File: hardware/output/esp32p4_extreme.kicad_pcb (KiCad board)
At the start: 4 copper layers, 110 x 80 mm, 234 parts, among them J1 USB-C, J2 USB-C, J3 USB-C, J4 RJ45 MagJack, J5 microSD, J6 2x12 header, J7 Fan 4P, J8 JST-SH 2P, J9 2x8 header, Q1 MMDT3904, Q2 AO3401A, Q3 AO3400A, Q4 AO3401A, Q5 AO3400A, Q6 AO3401A, SW1 Tactile, SW2 Tactile, U1 ESP32-P4NRW32X, U10 TPD4E05U06, U11 TPD4E05U06, U2 W25Q256JV 32MB, U3 TPS62130, U4 TLV62569, U5 LAN8720A, U6 CP2102N, U7 TPD2EUSB30, U8 USBLC6-2SC6, U9 USBLC6-2SC6, Y1 40MHz 10ppm, Y2 25MHz

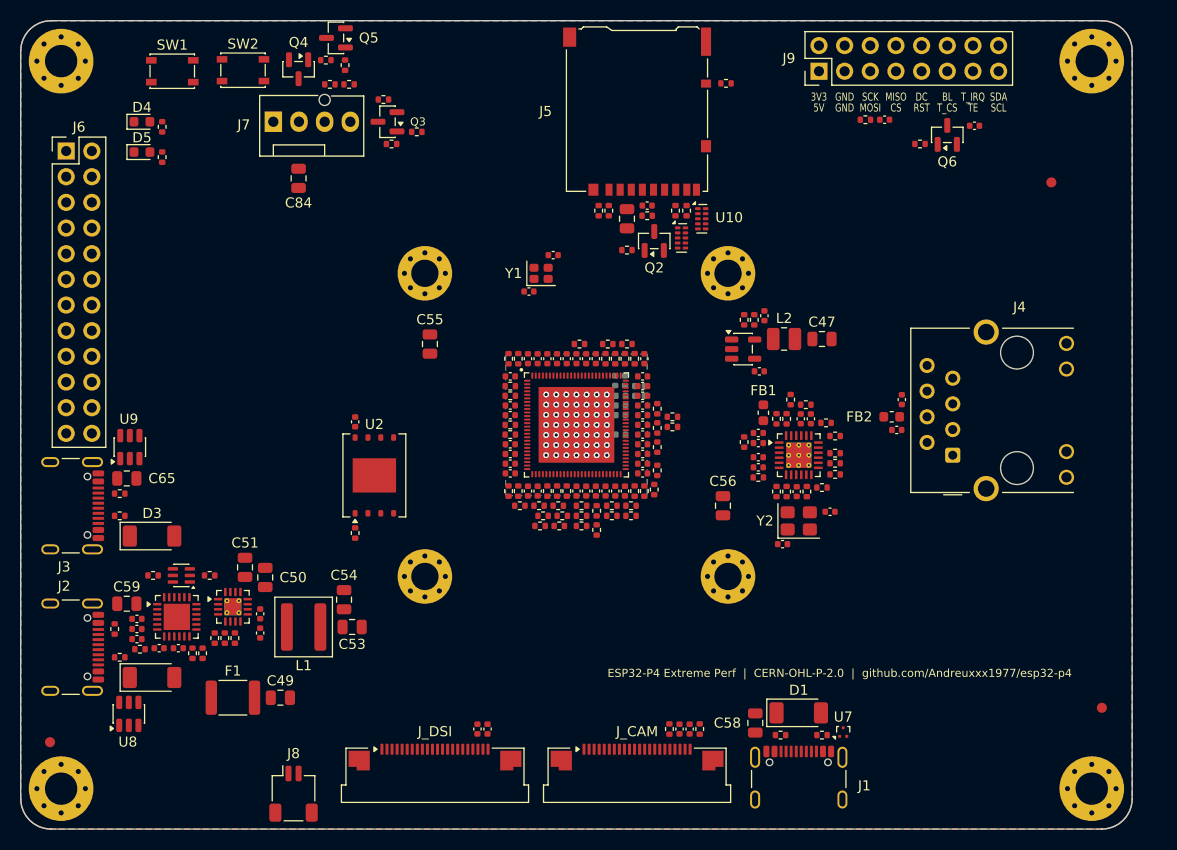
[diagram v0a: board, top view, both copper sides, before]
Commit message: Placement: keep a routable escape channel for every SoC pad; USB-C design tests
The first autorouting runs showed the SoC could not be escaped: the 0402 ring around
the 0.35 mm-pitch QFN left no gap >= 0.35 mm on any side, while ~60 of the 100 connected
pads go to parts outside it.

- layout_plan: new escape-channel model (section 5b). Each connected U1 pad gets a
  straight radial channel from the end of its fan-out stub; a top-side placement near
  the SoC is legal only if, per side and radial band, all channels still pack between
  the other nets' pads at netclass width + clearance (with a bounded 45-degree jog).
  Supply channels end at their first cap; series 0R/22R parts pass their own chain.
  U1 parts must sit in line with their own pad. The Hungarian ring-slot solver is
  replaced by the Near search under these rules (HF caps first).
- board_spec: first cap per pad within 2.1 mm, bulk caps within 4 mm, bias/strap
  within 7 mm, RMII/USJ source terminations within 8.5 mm, 0R links within 10 mm,
  XTAL links within 6.5 mm; 15 (was 8) caps on the bottom under the pad ring.
- Regenerated board, DRC rules and docs; KiCad 10 DRC still 0 errors (also for the
  board built through the pcbnew API).
- tests: escape channels stay open, SoC parts in line with their pad; new
  tests/test_usb_c.py checks all three USB-C ports end to end (Rd on each CC pin,
  both plug orientations, D+/D- polarity to the HS PHY / CP2102N / USB-Serial-JTAG,
  crossed UART, CP2102N VBUS divider and auto-program pair, ESD, VBUS OR-ing, 90 ohm
  pairs).
- autoroute: stubs end at the planner's U1_STUB_END_MM.

Co-Authored-By: Claude Opus 5.5 <noreply@anthropic.com>
Claude-Session: https://claude.ai/code/session_01HPbQMeq7CyuN5d7UYEJZ7D
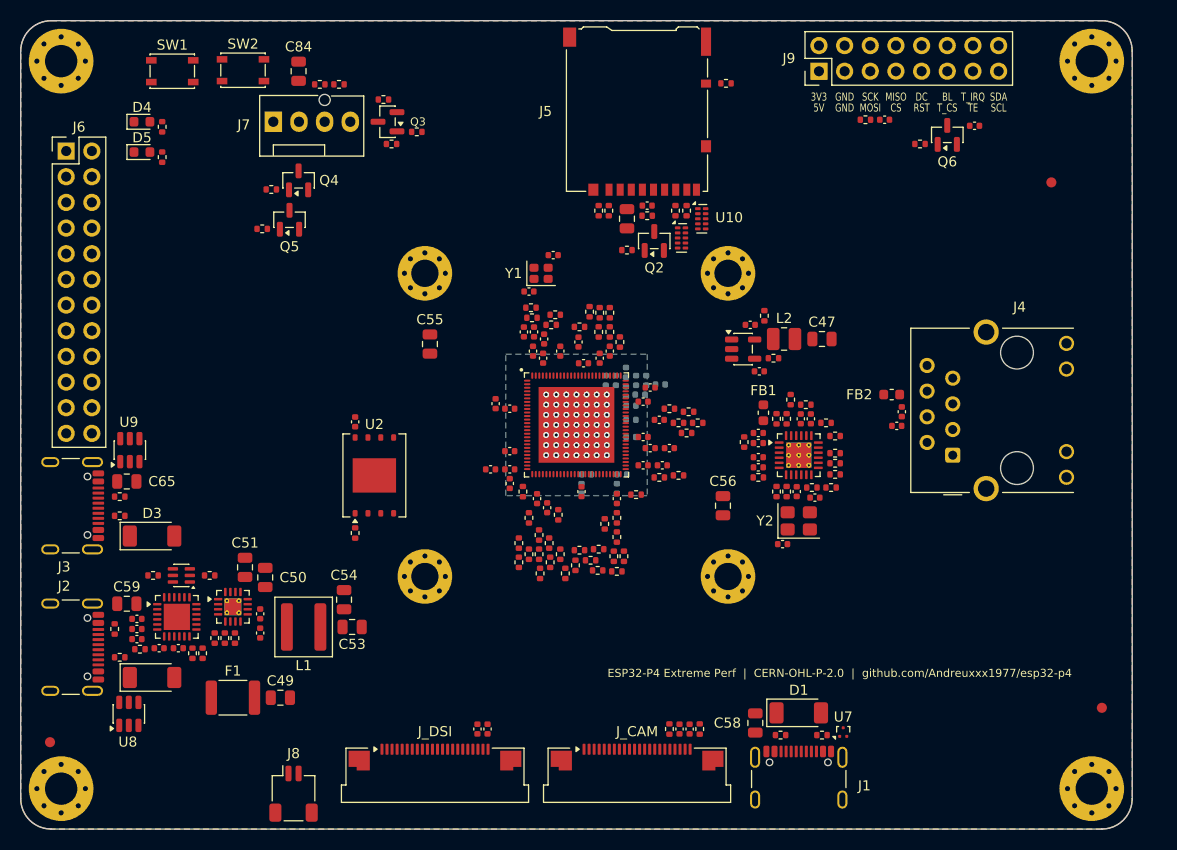
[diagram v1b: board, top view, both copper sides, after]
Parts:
- C10, C11, C13, C14, C25, C27, C32: moved to B.Cu
- moved Q5 18.6 mm to (120.1, 84.7), turned to 90 degrees
- moved R90 18.2 mm to (117.4, 85.6), turned to 0 degrees
- moved R89 13.9 mm to (118.3, 81.7), turned to 0 degrees
- moved R16 12.3 mm to (145.8, 116.7), turned to -90 degrees
- moved Q4 11.0 mm to (121.0, 80.8), turned to 90 degrees
- moved C84 10.6 mm to (121.0, 70.0), turned to 90 degrees
- moved R15 10.3 mm to (144.8, 115.9), turned to -90 degrees
- moved R12 9.17 mm to (146.4, 94.1), turned to 0 degrees
- moved R83 8.50 mm to (142.8, 118.6)
- moved R78 7.19 mm to (147.4, 119.7), turned to -90 degrees
- moved R2 7.09 mm to (144.1, 94.4)
- moved R17 7.06 mm to (145.9, 118.6)
- moved R77 5.70 mm to (152.5, 119.5), turned to 0 degrees
- moved R74 5.58 mm to (150.6, 119.4), turned to 180 degrees
- moved R6 5.52 mm to (144.0, 93.4), turned to 0 degrees
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
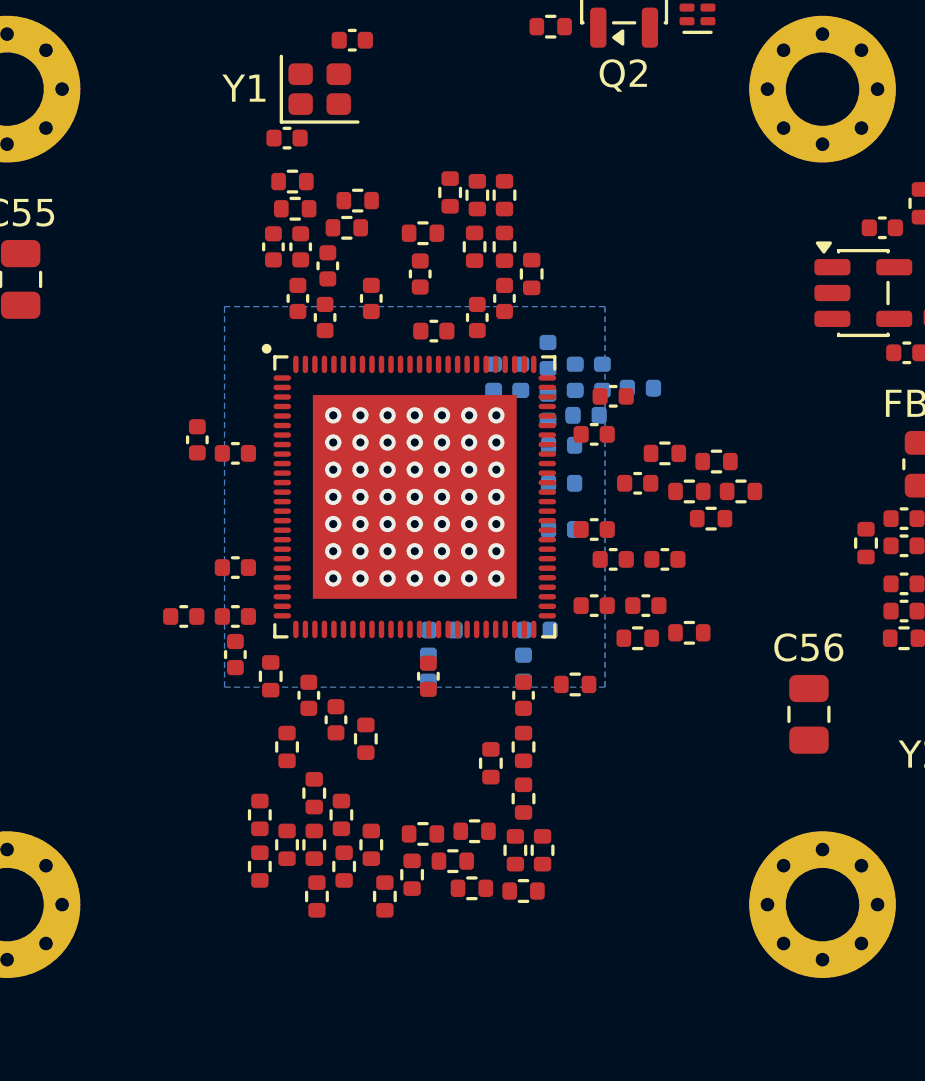
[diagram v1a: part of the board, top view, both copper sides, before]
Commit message: SoC escape tracks solved as a MILP; grid router to finish what the autorouter leaves
The router is not told about the escape-channel model and blocks channels (e.g. lays a
neighbour straight through the room a channel needed for its jog). So the escape tracks
are now routed by the planner itself and handed to the router as fixed copper:

- layout_plan: one mixed-integer program per SoC side (scipy/HiGHS): each channel's
  tangential position every 25 um of radius, starting on its pad line at the stub end,
  at most 45 degrees, netclass clearance to every other-net pad (exact point-to-rectangle
  distance, one binary per channel/pad for the side it passes), netclass pitch to the
  neighbours grown with the slope (parallel diagonals are closer than their tangential
  spacing), landing in the first own-net pad in line. Channels that cannot fit are
  dropped (left to the router). 74 of 100 are routed; escape_tracks.json is re-checked
  with exact segment geometry by the tests.
- The placer and the tracks now share one clearance model (the larger of the two nets'
  clearances, exact rounded ends), so the placement is only accepted where the tracks
  can really pass. Placement: no warnings; first cap per pad within 2.3 mm, bias/strap
  parts within 7.5 mm.
- autoroute: loads the escape tracks as locked pre-routing.
- tools/maze_route.py: grid router (exact copper distances, Dijkstra on both signal
  layers with through vias) for the unconnected items KiCad's DRC still reports;
  tools/finish_routing.py loops DRC -> grid router -> zone refill.
- requirements: numpy, scipy.

Co-Authored-By: Claude Opus 5.5 <noreply@anthropic.com>
Claude-Session: https://claude.ai/code/session_01HPbQMeq7CyuN5d7UYEJZ7D
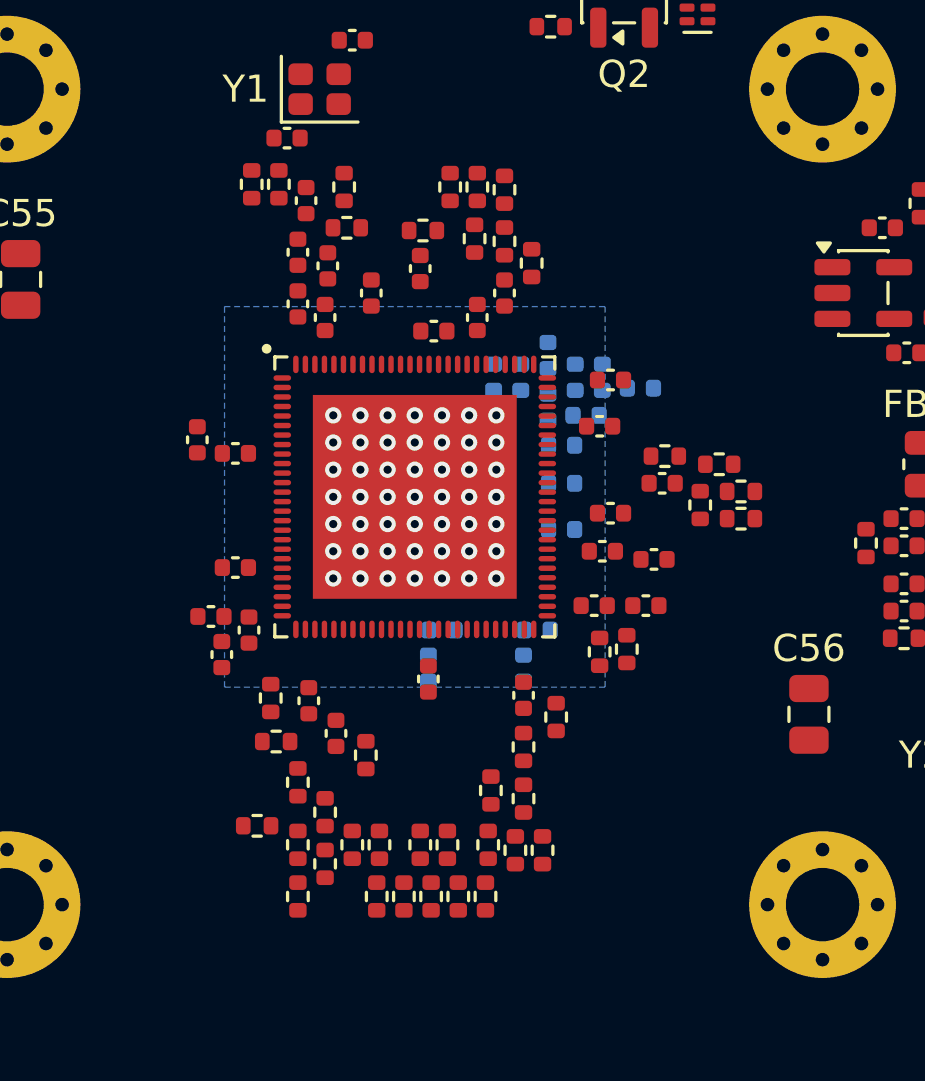
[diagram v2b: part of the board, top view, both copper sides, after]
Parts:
- moved R75 3.54 mm to (150.1, 119.7)
- moved R79 2.98 mm to (147.1, 119.7)
- moved R39 2.38 mm to (156.3, 110.6), turned to 90 degrees
- moved C42 2.08 mm to (144.5, 94.1)
- moved R81 2.02 mm to (144.2, 117.8)
- moved C6 1.98 mm to (141.4, 110.8), turned to -90 degrees
- moved R83 1.78 mm to (144.2, 119.7)
- moved C5 1.66 mm to (141.0, 109.4), turned to 180 degrees
- moved R77 1.66 mm to (153.2, 118.0), turned to -90 degrees
- moved R80 1.57 mm to (145.2, 118.5)
- moved R6 1.50 mm to (142.5, 93.5), turned to 90 degrees
- moved R9 1.49 mm to (160.5, 104.8)
- moved R3 1.49 mm to (155.3, 110.7), turned to 90 degrees
- moved R40 1.39 mm to (153.7, 113.1), turned to 90 degrees
- moved R73 1.34 mm to (148.7, 117.8), turned to -90 degrees
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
